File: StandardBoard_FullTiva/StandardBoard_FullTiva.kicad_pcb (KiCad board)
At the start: 2 copper layers, 124.5 x 89.9 mm, 2 parts

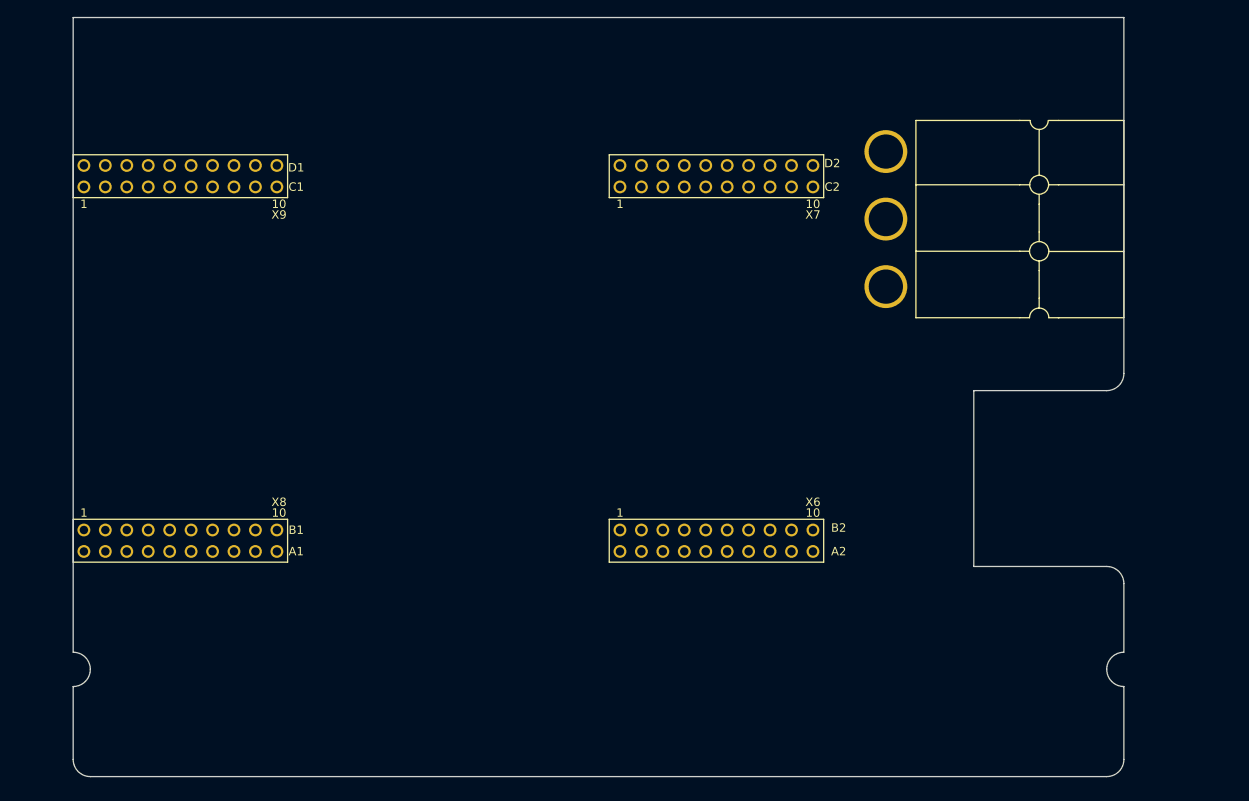
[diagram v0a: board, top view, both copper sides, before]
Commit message: Moified Silkscreen
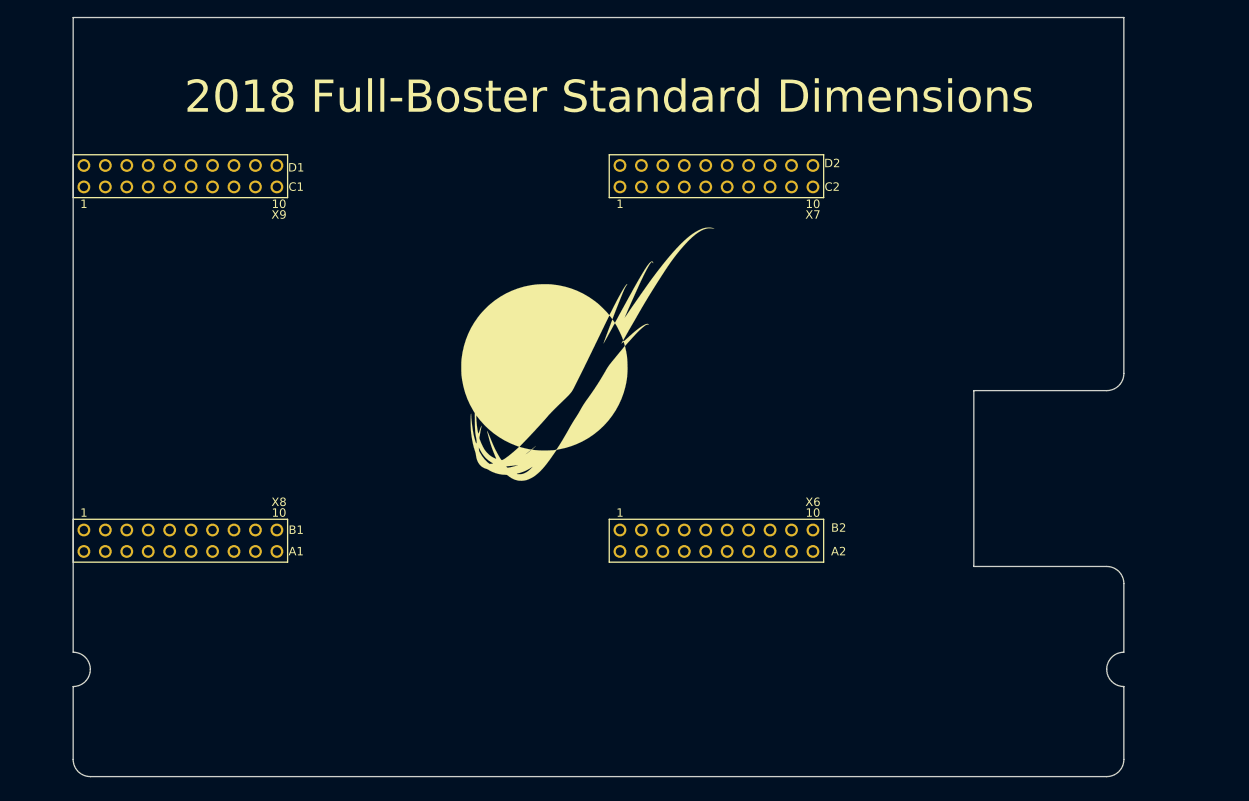
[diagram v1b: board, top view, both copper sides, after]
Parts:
- removed the REF** at (191.3, 66.3)
- added G***: LOGO, MRDT_Silkscreens:MRDT_Logo_30mm, F.Cu at (152.4, 94.0)
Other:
- board text added: "2018 Full-Boster Standard Dimensions"

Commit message: Added silksceen and generated gerbs
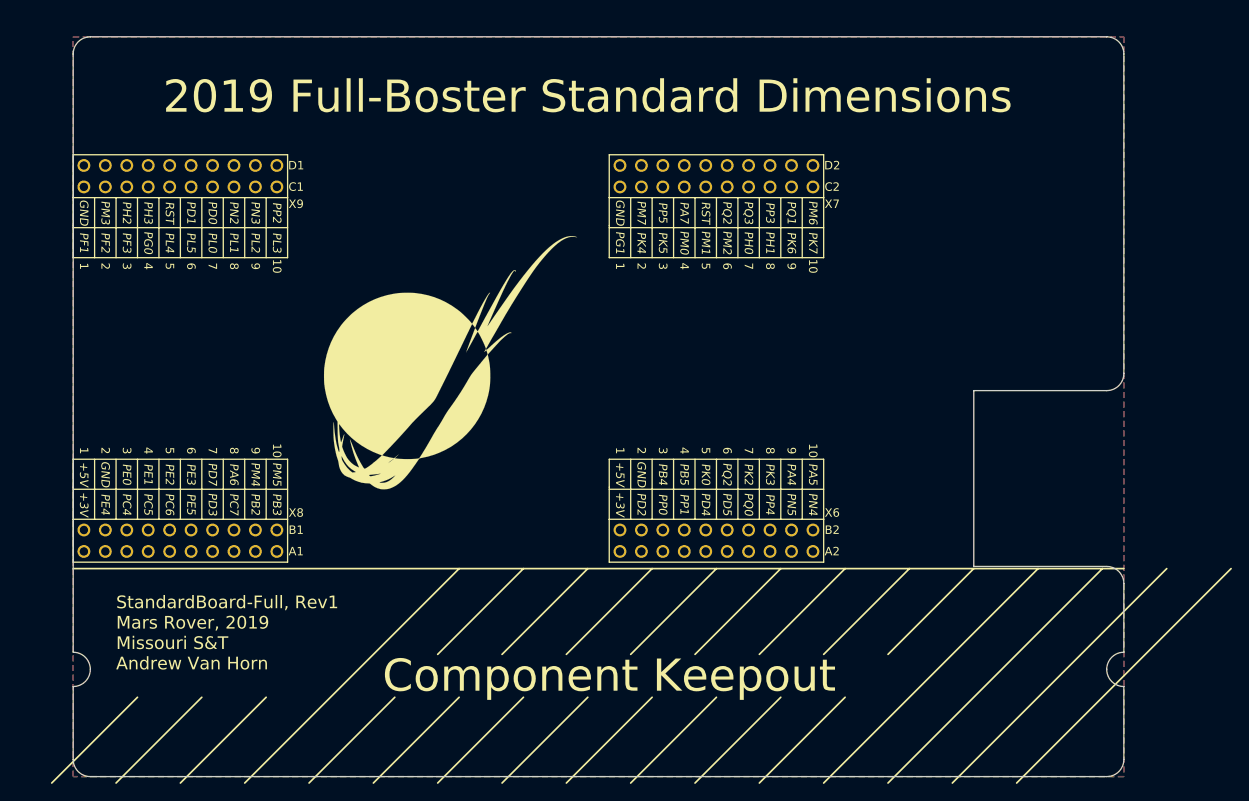
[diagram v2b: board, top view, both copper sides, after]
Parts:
- moved G*** 16.3 mm to (136.1, 95.0)
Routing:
- added copper zone on B.Cu, net (none)
- added copper zone on F.Cu, net (none)
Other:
- board size 124.5 x 89.9 mm -> 124.5 x 87.6 mm
- board text added: "+3V"
- board text added: "+5V"
- board text added: "-->"
- board text added: "1"
- board text added: "10"
- board text added: "2"
- board text added: "2019 Full-Boster Standard Dimensions"
- board text added: "3"
- board text added: "4"
- board text added: "5"
- board text added: "6"
- board text added: "7"
- board text added: "8"
- board text added: "9"
- board text added: "A1"
- board text added: "A2"
- board text added: "B1"
- board text added: "B2"
- board text added: "Board May Extend This Way"
- board text added: "C1"
- board text added: "C2"
- board text added: "Component Keepout"
- board text added: "D1"
- board text added: "D2"
- board text added: "GND"
- board text added: "PA4"
- board text added: "PA5"
- board text added: "PA6"
- board text added: "PA7"
- board text added: "PB2"
- board text added: "PB3"
- board text added: "PB4"
- board text added: "PB5"
- board text added: "PC4"
- board text added: "PC5"
- board text added: "PC6"
- board text added: "PC7"
- board text added: "PD0"
- board text added: "PD1"
- board text added: "PD2"
- board text added: "PD3"
- board text added: "PD4"
- board text added: "PD5"
- board text added: "PD7"
- board text added: "PE0"
- board text added: "PE1"
- board text added: "PE2"
- board text added: "PE3"
- board text added: "PE4"
- board text added: "PE5"
- board text added: "PF1"
- board text added: "PF2"
- board text added: "PF3"
- board text added: "PG0"
- board text added: "PG1"
- board text added: "PH0"
- board text added: "PH1"
- board text added: "PH2"
- board text added: "PH3"
- board text added: "PK0"
- board text added: "PK2"
- board text added: "PK3"
- board text added: "PK4"
- board text added: "PK5"
- board text added: "PK6"
- board text added: "PK7"
- board text added: "PL0"
- board text added: "PL1"
- board text added: "PL2"
- board text added: "PL3"
- board text added: "PL4"
- board text added: "PL5"
- board text added: "PM0"
- board text added: "PM1"
- board text added: "PM2"
- board text added: "PM3"
- board text added: "PM4"
- board text added: "PM5"
- board text added: "PM6"
- board text added: "PM7"
- board text added: "PN2"
- board text added: "PN3"
- board text added: "PN4"
- board text added: "PN5"
- board text added: "PP0"
- board text added: "PP1"
- board text added: "PP2"
- board text added: "PP3"
- board text added: "PP4"
- board text added: "PP5"
- board text added: "PQ0"
- board text added: "PQ1"
- board text added: "PQ2"
- board text added: "PQ3"
- board text added: "RST"
- board text added: "StandardBoard-Full, Rev1 Mars Rover, 2019 Missouri S&T Andrew Van Horn"
- board text added: "X6"
- board text added: "X7"
- board text added: "X8"
- board text added: "X9"
- board text removed: "2018 Full-Boster Standard Dimensions"
